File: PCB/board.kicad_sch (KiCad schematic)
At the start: 172 parts, among them J1 Micro_SD_Card, J10 Conn_01x10, J11 Conn_01x02, J12 Conn_02x04_Odd_Even, J13 Conn_01x02, J14 Conn_01x02, J15 Conn_01x03, J16 Conn_01x02, J17 Conn_01x05, J18 Conn_01x04, J19 Conn_01x04, J2 Conn_ARM_JTAG_SWD_10, J20 Conn_01x02, J21 Conn_01x03, J22 Conn_02x04_Odd_Even, J23 Conn_01x04, J24 Conn_01x04, J25 Conn_01x02, J26 Conn_01x03, J27 Conn_02x04_Odd_Even, J28 Conn_01x04, J29 Conn_01x04, J30 Conn_01x02, J31 Conn_01x03, J32 Conn_01x02, J33 Conn_01x02, J34 Conn_01x02, J35 Conn_01x02, J36 Conn_01x02, J37 Conn_01x02, J4 Conn_01x04, J5 Conn_01x04, J6 Conn_01x02, J7 Conn_01x03, J8 Conn_02x04_Odd_Even, J9 Conn_01x10, P1 USB_C_Plug_USB2.0, Q1 IRLML6402, Q2 NMOS, Q3 NMOS, Q4 NMOS, Q5 NMOS, Q6 NMOS, SW1 SW_Push, SW2 SW_Push, U1 STM32H743VITx, U2 AMS1117-3.3, U3 TPS54331, U4 TMC2209_SILENTSTEPSTICK, U5 TMC2209_SILENTSTEPSTICK, U6 TMC2209_SILENTSTEPSTICK, U7 TMC2209_SILENTSTEPSTICK, Y1 25 MHz

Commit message: added TMC footprint to the drivers
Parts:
- U4, U5, U6, U7: footprint TMC2209_SILENTSTEPSTICK:MODULE_TMC2209_SILENTSTEPSTICK -> kai's library:TMC Stepstick
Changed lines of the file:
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@@
 			)
 		)
-		(property "Footprint" "TMC2209_SILENTSTEPSTICK:MODULE_TMC2209_SILENTSTEPSTICK"
+		(property "Footprint" "kai's library:TMC Stepstick"
 			(at 330.2 105.41 0)
 			(effects
@@
 			)
 		)
-		(property "Footprint" "TMC2209_SILENTSTEPSTICK:MODULE_TMC2209_SILENTSTEPSTICK"
+		(property "Footprint" "kai's library:TMC Stepstick"
 			(at 330.2 234.95 0)
 			(effects
@@
 			)
 		)
-		(property "Footprint" "TMC2209_SILENTSTEPSTICK:MODULE_TMC2209_SILENTSTEPSTICK"
+		(property "Footprint" "kai's library:TMC Stepstick"
 			(at 330.2 170.18 0)
 			(effects
@@
 			)
 		)
-		(property "Footprint" "TMC2209_SILENTSTEPSTICK:MODULE_TMC2209_SILENTSTEPSTICK"
+		(property "Footprint" "kai's library:TMC Stepstick"
 			(at 330.2 40.64 0)
 			(effects

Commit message: changed some footprints to handle the loads
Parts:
- D1: footprint Diode_SMD:D_2114_3652Metric -> Diode_SMD:D_SMA
- D13, D15: footprint Diode_SMD:D_SMA -> Package_TO_SOT_THT:TO-220-2_Vertical
- D2: footprint Package_TO_SOT_THT:TO-220-2_Horizontal_TabDown -> Package_TO_SOT_THT:TO-220-2_Vertical
- R12, R13: footprint Resistor_SMD:R_0603_1608Metric -> Resistor_SMD:R_0805_2012Metric
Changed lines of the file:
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@@
 			)
 		)
-		(property "Footprint" "Package_TO_SOT_THT:TO-220-2_Horizontal_TabDown"
+		(property "Footprint" "Package_TO_SOT_THT:TO-220-2_Vertical"
 			(at 77.47 27.94 0)
 			(effects
@@
 			)
 		)
-		(property "Footprint" "Diode_SMD:D_2114_3652Metric"
+		(property "Footprint" "Diode_SMD:D_SMA"
 			(at 46.99 31.75 0)
 			(effects
@@
 			)
 		)
-		(property "Footprint" "Diode_SMD:D_SMA"
+		(property "Footprint" "Package_TO_SOT_THT:TO-220-2_Vertical"
 			(at 209.55 193.04 0)
 			(effects
@@
 			)
 		)
-		(property "Footprint" "Resistor_SMD:R_0603_1608Metric"
+		(property "Footprint" "Resistor_SMD:R_0805_2012Metric"
 			(at 60.452 54.61 90)
 			(effects
@@
 			)
 		)
-		(property "Footprint" "Diode_SMD:D_SMA"
+		(property "Footprint" "Package_TO_SOT_THT:TO-220-2_Vertical"
 			(at 254 193.04 0)
 			(effects
@@
 			)
 		)
-		(property "Footprint" "Resistor_SMD:R_0603_1608Metric"
+		(property "Footprint" "Resistor_SMD:R_0805_2012Metric"
 			(at 60.452 63.5 90)
 			(effects

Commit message: fixing the footprint for the motor drivers
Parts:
- J18, J23, J28, J4: footprint Connector_JST:JST_VH_B4P-VH_1x04_P3.96mm_Vertical -> Connector_JST:JST_XH_B4B-XH-AM_1x04_P2.50mm_Vertical
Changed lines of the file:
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@@
 			)
 		)
-		(property "Footprint" "Connector_JST:JST_VH_B4P-VH_1x04_P3.96mm_Vertical"
+		(property "Footprint" "Connector_JST:JST_XH_B4B-XH-AM_1x04_P2.50mm_Vertical"
 			(at 354.33 105.41 0)
 			(effects
@@
 			)
 		)
-		(property "Footprint" "Connector_JST:JST_VH_B4P-VH_1x04_P3.96mm_Vertical"
+		(property "Footprint" "Connector_JST:JST_XH_B4B-XH-AM_1x04_P2.50mm_Vertical"
 			(at 354.33 40.64 0)
 			(effects
@@
 			)
 		)
-		(property "Footprint" "Connector_JST:JST_VH_B4P-VH_1x04_P3.96mm_Vertical"
+		(property "Footprint" "Connector_JST:JST_XH_B4B-XH-AM_1x04_P2.50mm_Vertical"
 			(at 354.33 170.18 0)
 			(effects
@@
 			)
 		)
-		(property "Footprint" "Connector_JST:JST_VH_B4P-VH_1x04_P3.96mm_Vertical"
+		(property "Footprint" "Connector_JST:JST_XH_B4B-XH-AM_1x04_P2.50mm_Vertical"
 			(at 354.33 234.95 0)
 			(effects

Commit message: fixed all the connectors except the LCD/TFT ones
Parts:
- J13, J14, J6: footprint Connector_JST:JST_XH_B2B-XH-A_1x02_P2.50mm_Vertical -> Connector_JST:JST_PH_B2B-PH-K_1x02_P2.00mm_Vertical
- J32, J33, J34: footprint Connector_JST:JST_XH_B3B-XH-A_1x03_P2.50mm_Vertical -> Connector_JST:JST_PH_B2B-PH-K_1x02_P2.00mm_Vertical
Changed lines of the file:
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@@
 			)
 		)
-		(property "Footprint" "Connector_JST:JST_XH_B2B-XH-A_1x02_P2.50mm_Vertical"
+		(property "Footprint" "Connector_JST:JST_PH_B2B-PH-K_1x02_P2.00mm_Vertical"
 			(at 107.95 154.94 0)
 			(effects
@@
 			)
 		)
-		(property "Footprint" "Connector_JST:JST_XH_B2B-XH-A_1x02_P2.50mm_Vertical"
+		(property "Footprint" "Connector_JST:JST_PH_B2B-PH-K_1x02_P2.00mm_Vertical"
 			(at 67.31 154.94 0)
 			(effects
@@
 			)
 		)
-		(property "Footprint" "Connector_JST:JST_XH_B3B-XH-A_1x03_P2.50mm_Vertical"
+		(property "Footprint" "Connector_JST:JST_PH_B2B-PH-K_1x02_P2.00mm_Vertical"
 			(at 21.59 232.41 0)
 			(effects
@@
 			)
 		)
-		(property "Footprint" "Connector_JST:JST_XH_B2B-XH-A_1x02_P2.50mm_Vertical"
+		(property "Footprint" "Connector_JST:JST_PH_B2B-PH-K_1x02_P2.00mm_Vertical"
 			(at 26.67 154.94 0)
 			(effects
@@
 			)
 		)
-		(property "Footprint" "Connector_JST:JST_XH_B3B-XH-A_1x03_P2.50mm_Vertical"
+		(property "Footprint" "Connector_JST:JST_PH_B2B-PH-K_1x02_P2.00mm_Vertical"
 			(at 110.49 232.41 0)
 			(effects
@@
 			)
 		)
-		(property "Footprint" "Connector_JST:JST_XH_B3B-XH-A_1x03_P2.50mm_Vertical"
+		(property "Footprint" "Connector_JST:JST_PH_B2B-PH-K_1x02_P2.00mm_Vertical"
 			(at 66.04 232.41 0)
 			(effects

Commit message: added the display connectors, finally!
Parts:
- J10, J9: footprint Connector_PinHeader_2.54mm:PinHeader_2x05_P2.54mm_Vertical -> Connector_IDC:IDC-Header_2x05-1MP_P2.54mm_Latch6.5mm_Vertical
- J17: footprint Connector_PinHeader_2.54mm:PinHeader_1x05_P2.54mm_Vertical -> Connector_JST:JST_XH_B5B-XH-AM_1x05_P2.50mm_Vertical
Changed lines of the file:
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@@
 			)
 		)
-		(property "Footprint" "Connector_PinHeader_2.54mm:PinHeader_2x05_P2.54mm_Vertical"
+		(property "Footprint" "Connector_IDC:IDC-Header_2x05-1MP_P2.54mm_Latch6.5mm_Vertical"
 			(at 144.78 194.31 0)
 			(effects
@@
 			)
 		)
-		(property "Footprint" "Connector_PinHeader_2.54mm:PinHeader_1x05_P2.54mm_Vertical"
+		(property "Footprint" "Connector_JST:JST_XH_B5B-XH-AM_1x05_P2.50mm_Vertical"
 			(at 93.98 194.31 0)
 			(effects
@@
 			)
 		)
-		(property "Footprint" "Connector_PinHeader_2.54mm:PinHeader_2x05_P2.54mm_Vertical"
+		(property "Footprint" "Connector_IDC:IDC-Header_2x05-1MP_P2.54mm_Latch6.5mm_Vertical"
 			(at 121.92 194.31 0)
 			(effects

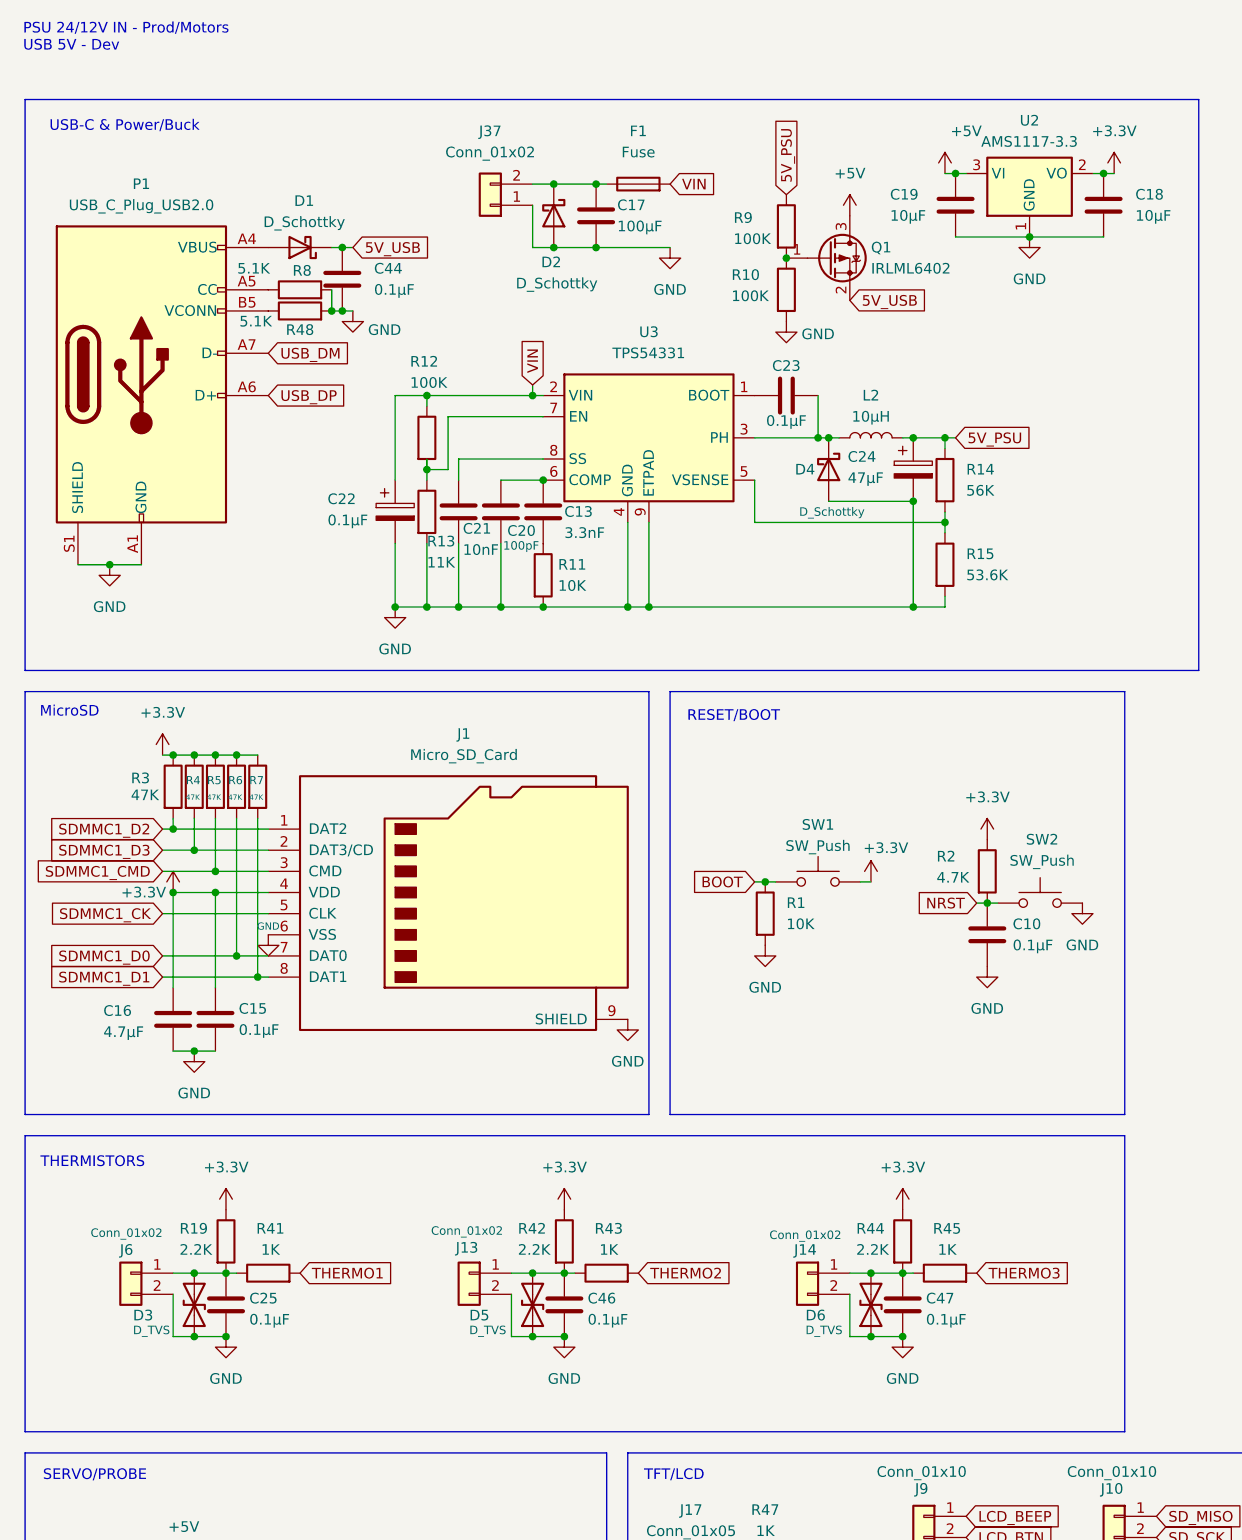
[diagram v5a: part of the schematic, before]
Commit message: simplifying the BOM
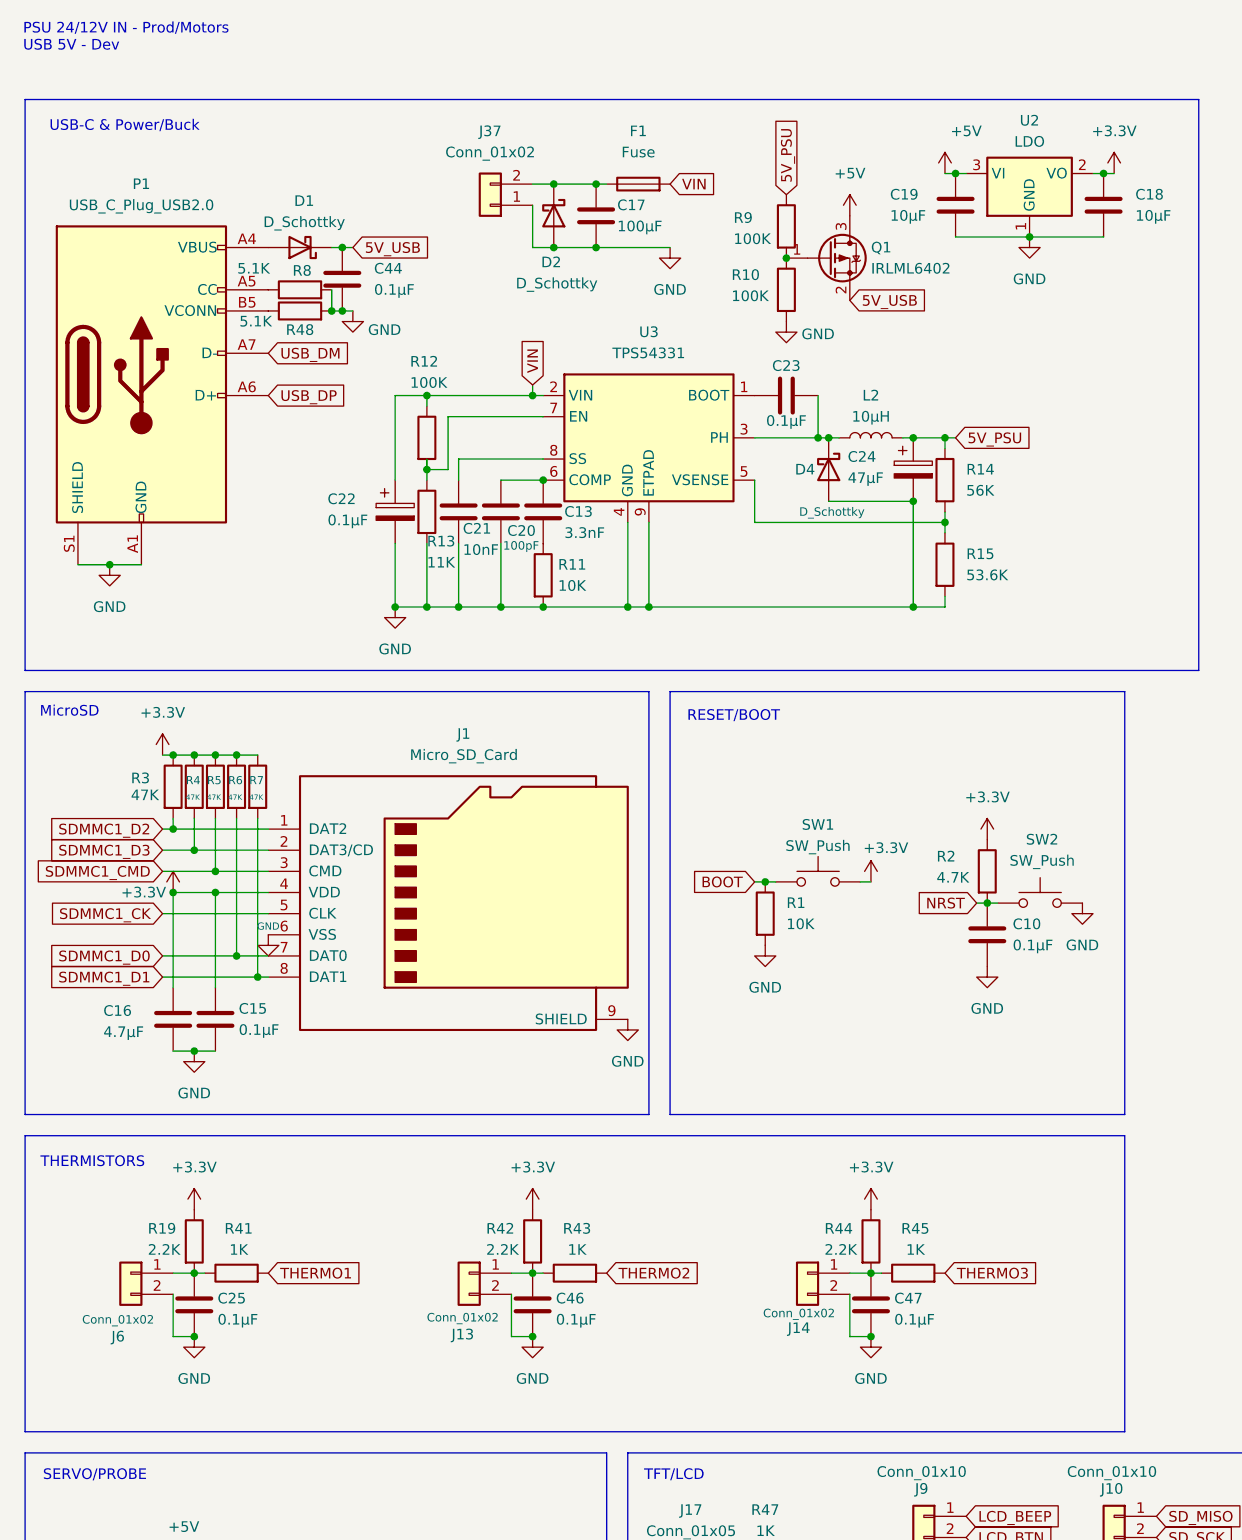
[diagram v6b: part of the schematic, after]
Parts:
- removed D3, D5, D6: D_TVS, Diode_SMD:D_SOD-323, symbol Device:D_TVS
- U2: value AMS1117-3.3 -> LDO
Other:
- moved on the sheet: C25, C46, C47, R19, R41, R42, R43, R44, R45

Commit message: cleaner up some stuff, this would be a good commit to revert too
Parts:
- U4, U5, U6, U7: value TMC2209_SILENTSTEPSTICK -> TMC Stepstick
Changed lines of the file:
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@@
 			)
 		)
-		(property "Value" "TMC2209_SILENTSTEPSTICK"
+		(property "Value" "TMC Stepstick"
 			(at 330.2 82.55 0)
 			(effects
@@
 			)
 		)
-		(property "Value" "TMC2209_SILENTSTEPSTICK"
+		(property "Value" "TMC Stepstick"
 			(at 330.2 212.09 0)
 			(effects
@@
 			)
 		)
-		(property "Value" "TMC2209_SILENTSTEPSTICK"
+		(property "Value" "TMC Stepstick"
 			(at 330.2 147.32 0)
 			(effects
@@
 			)
 		)
-		(property "Value" "TMC2209_SILENTSTEPSTICK"
+		(property "Value" "TMC Stepstick"
 			(at 330.2 17.78 0)
 			(effects
